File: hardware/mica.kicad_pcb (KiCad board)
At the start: 2 copper layers, 100 x 100 mm, 145 parts, among them J1 USB_C_Receptacle_USB2.0, J2 Conn_ARM_JTAG_SWD_10, SW1 SW_User, U1 STM32F072C8Tx, U10 LMP7715, U2 MIC5205-3.3YM5, U3 LMP7715, U4 LMP7715, U5 LMP7715, U6 LMP7715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

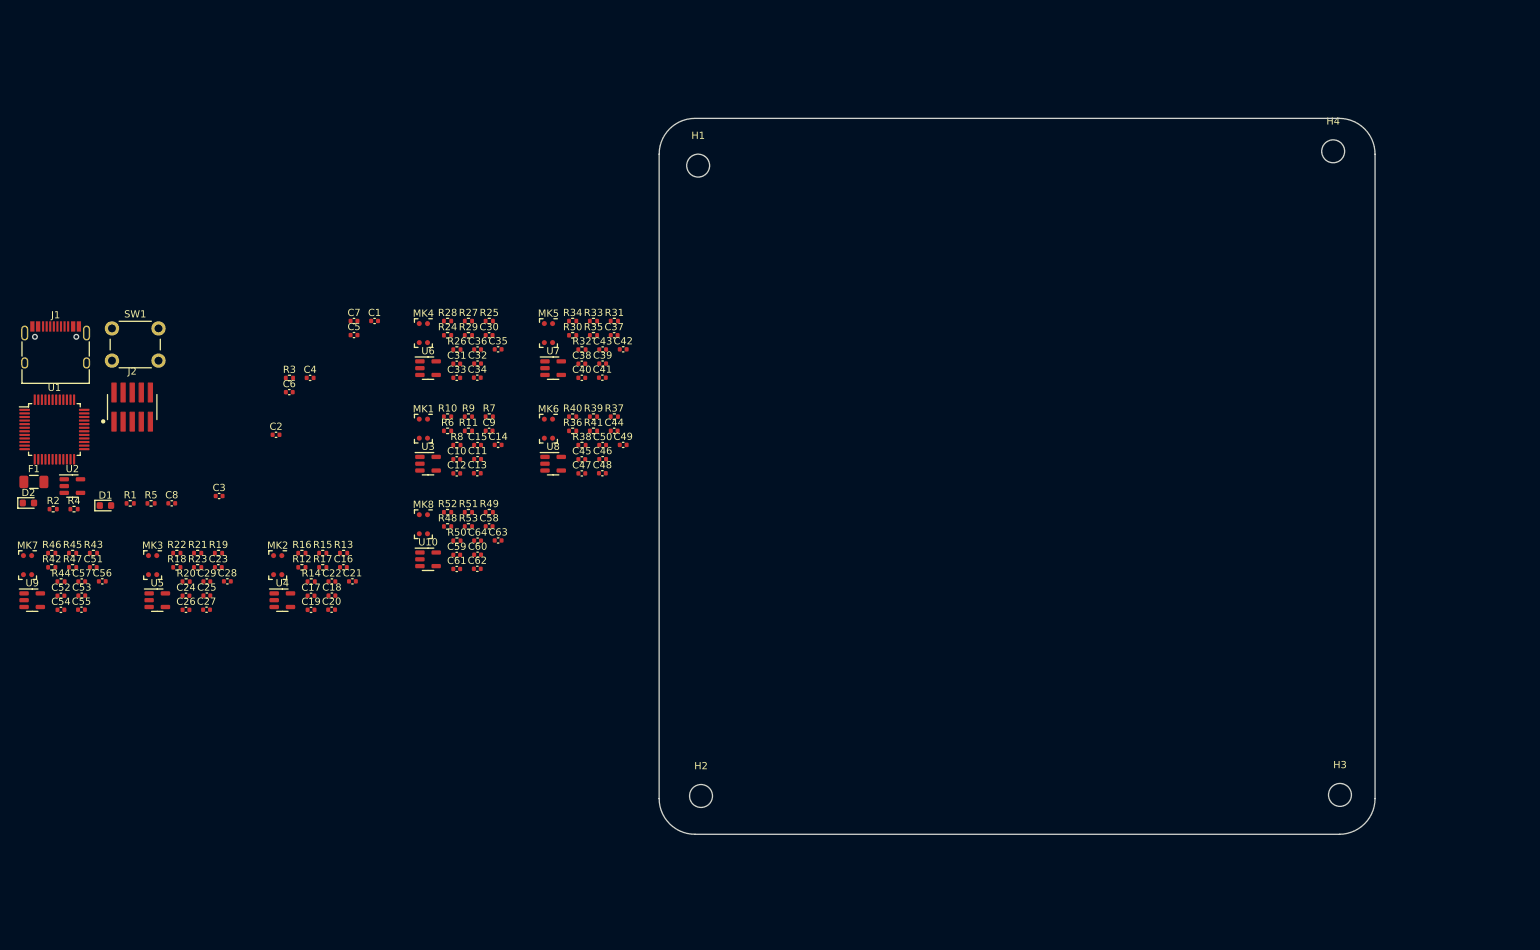
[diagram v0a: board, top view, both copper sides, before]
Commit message: Place every component except microphones + amplifiers
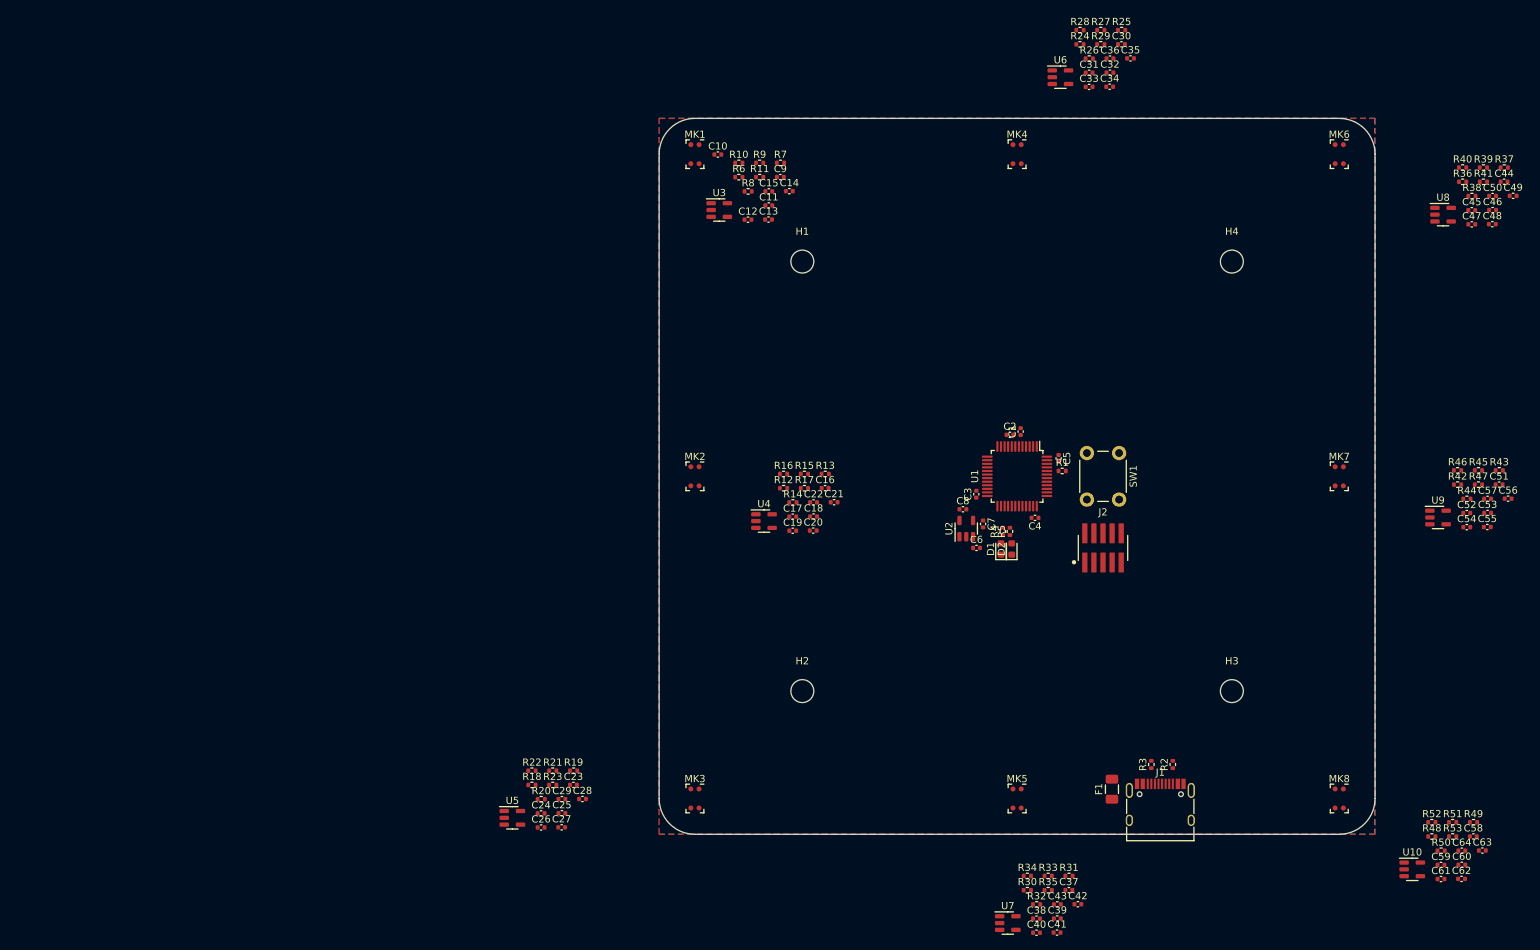
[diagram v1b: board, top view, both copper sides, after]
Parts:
- moved C51 196.7 mm to (217.3, 101.2)
- moved C52 196.7 mm to (212.8, 105.1)
- moved C53 196.7 mm to (215.7, 105.1)
- moved C54 196.7 mm to (212.8, 107.1)
- moved C55 196.7 mm to (215.7, 107.1)
- moved C56 196.7 mm to (218.6, 103.1)
- moved C57 196.7 mm to (215.7, 103.1)
- moved R42 196.7 mm to (211.5, 101.2)
- moved R43 196.7 mm to (217.3, 99.2)
- moved R44 196.7 mm to (212.8, 103.2)
- moved R45 196.7 mm to (214.4, 99.2)
- moved R46 196.7 mm to (211.5, 99.2)
- moved R47 196.7 mm to (214.4, 101.2)
- moved U9 196.7 mm to (208.8, 105.8)
- moved MK7 183.6 mm to (195.0, 100.0)
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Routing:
- added copper zone on F.Cu, net +3V3
- added copper zone on B.Cu, net GND
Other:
- outline, holes or cut-outs redrawn

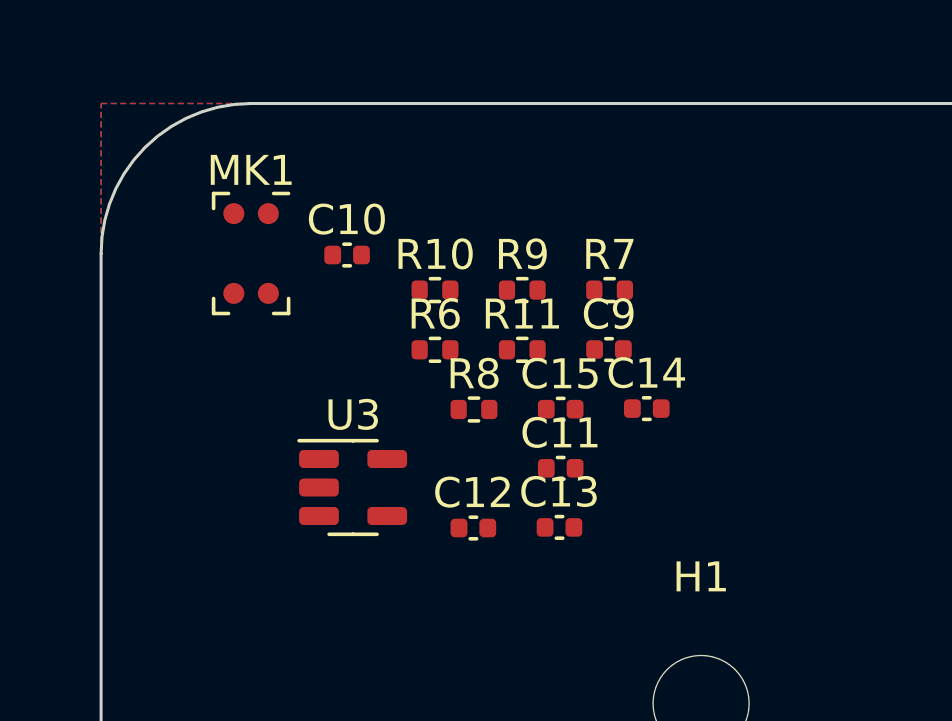
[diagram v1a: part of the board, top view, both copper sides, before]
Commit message: Place microphone + amplifier components
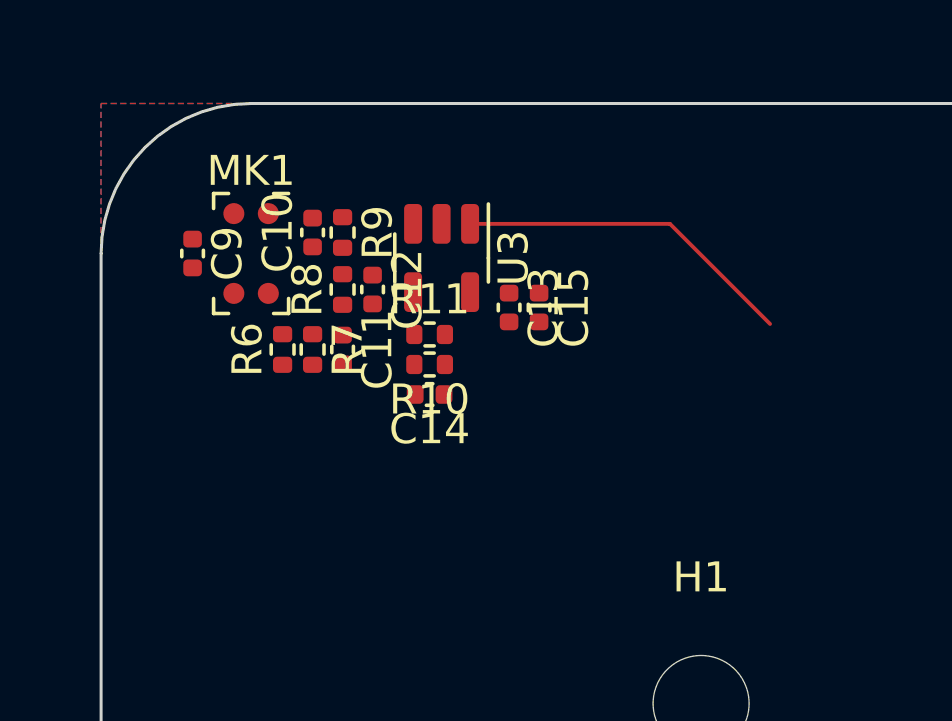
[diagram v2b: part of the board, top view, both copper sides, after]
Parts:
- moved C9 14.2 mm to (103.0, 55.0), turned to -90 degrees
- moved R7 10.1 mm to (107.0, 58.2), turned to -90 degrees
- moved C12 8.63 mm to (109.0, 56.2), turned to -90 degrees
- moved C11 8.28 mm to (108.0, 58.2), turned to -90 degrees
- moved U3 8.20 mm to (111.3, 55.1), turned to -90 degrees
- moved C13 7.52 mm to (113.6, 56.8), turned to -90 degrees
- moved C14 7.26 mm to (111.0, 59.7), turned to 180 degrees
- moved R9 6.29 mm to (108.0, 54.3), turned to -90 degrees
- moved R8 5.93 mm to (108.0, 56.2), turned to 90 degrees
- moved R6 5.08 mm to (106.0, 58.2), turned to 90 degrees
- moved C15 3.47 mm to (114.6, 56.8), turned to -90 degrees
- moved R11 3.13 mm to (111.0, 57.7)
- moved R10 2.49 mm to (111.0, 58.7), turned to 180 degrees
- moved C10 1.37 mm to (107.0, 54.3), turned to 90 degrees
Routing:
- net /MIC1: track 0.00 -> 11.4 mm
